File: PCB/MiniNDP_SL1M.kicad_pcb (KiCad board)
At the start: 2 copper layers, 60 x 34 mm, 22 parts, among them J1 Conn_02x20_Odd_Even, U1 AS6C8008_TSOPII, U2 HC238, U3 HC4040, U4 ABT841

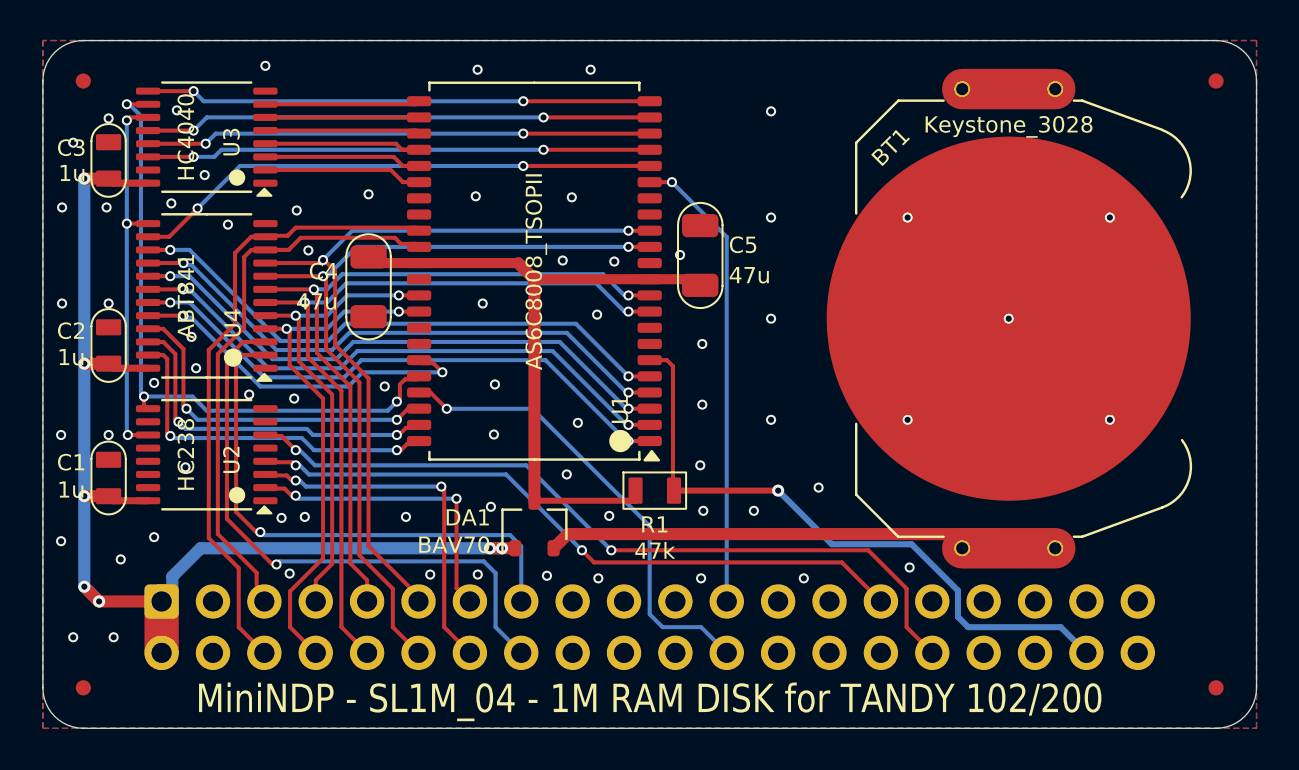
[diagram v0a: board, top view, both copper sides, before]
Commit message: minindp ez1m sl1m ez512 u1m pcbs trace spacing & gnd paths
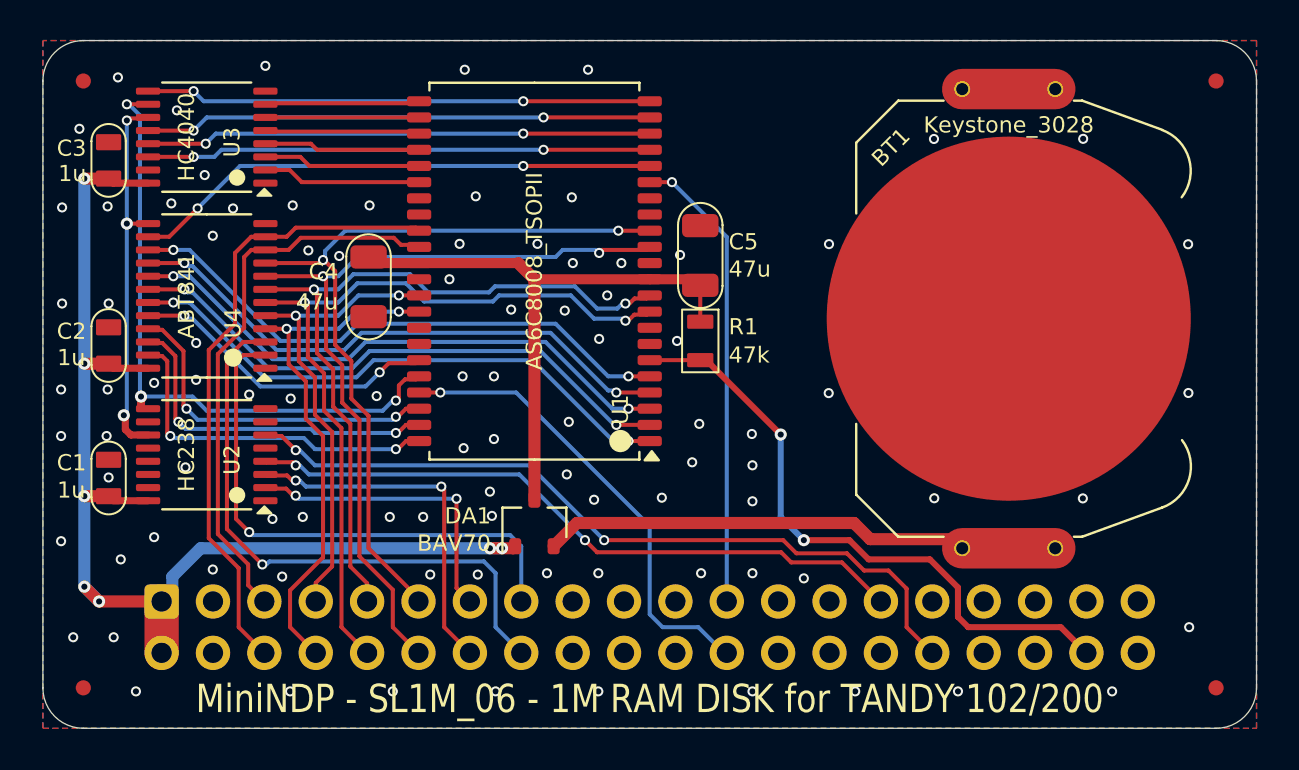
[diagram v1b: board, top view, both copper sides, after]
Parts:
- moved R1 7.73 mm to (154.4, 100.9), turned to -90 degrees
- moved DA1 0.10 mm to (146.2, 109.9)
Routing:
- net VMEM: track 33.5 -> 29.7 mm
- net /A13: track 17.7 -> 15.4 mm
- net +BATT: track 23.1 -> 21.2 mm
- net /RAMRST: track 31.9 -> 30.8 mm, vias 1 -> 2
- net /AD5: track 36.3 -> 37.1 mm
- net /AD4: track 38.6 -> 39.2 mm
- net GND: vias 69 -> 94

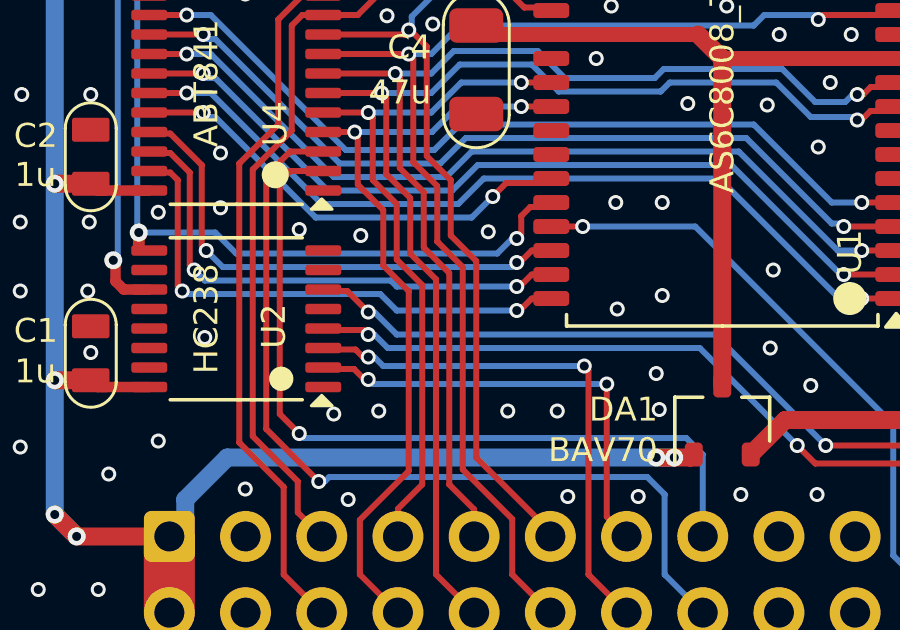
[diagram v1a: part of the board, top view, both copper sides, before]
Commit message: rename breadboard, sl1m trace spacing & silkscreen
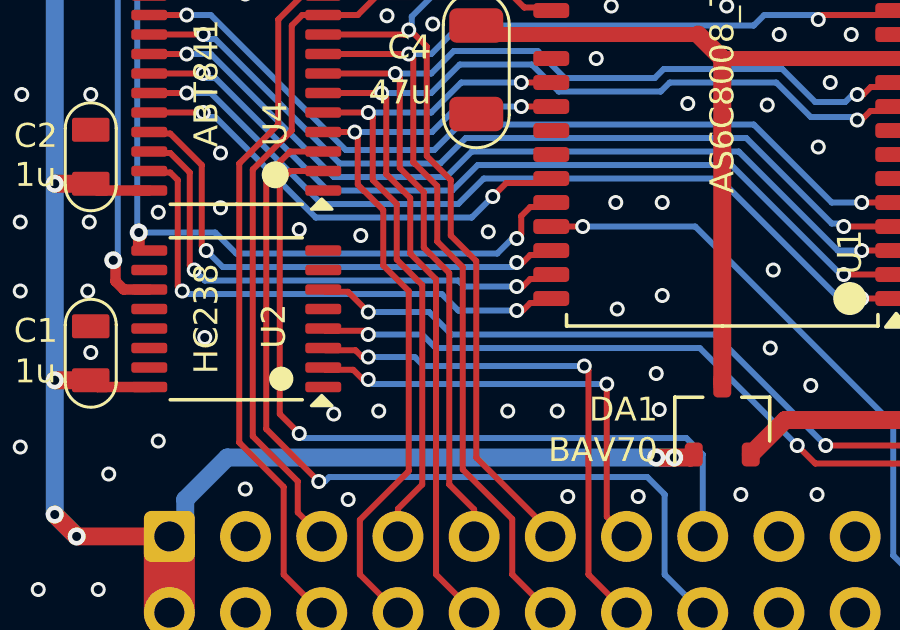
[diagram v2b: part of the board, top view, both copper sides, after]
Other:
- board text added: "To reinstall RAMDSK from device after hard reset. RAMxxx.CO must be the first file in bank 0."
- board text removed: "Bootstrap RAMDSK from BANK 0. For BANK 1 change OUT129 to OUT133. RAM100.CO or RAM200.CO must be the first file in the bank."

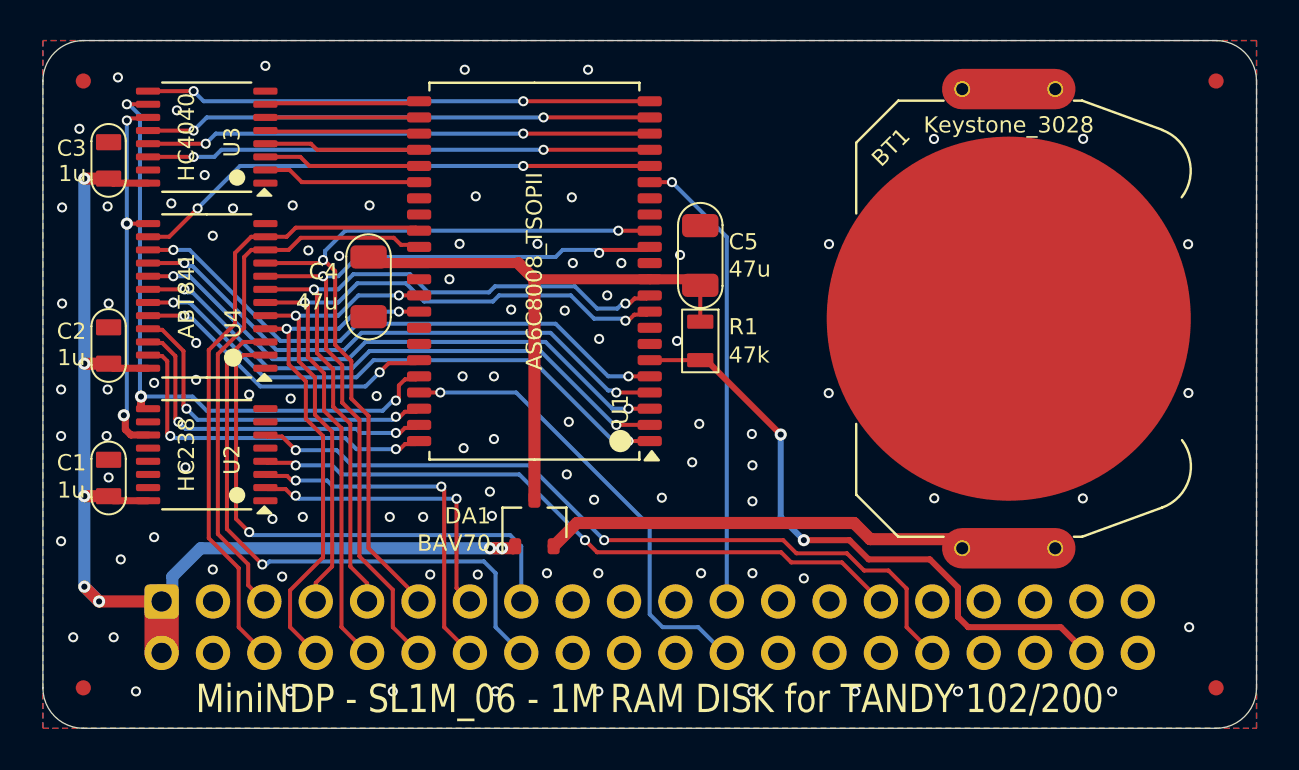
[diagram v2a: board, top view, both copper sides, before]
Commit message: sl1m fillet tracks
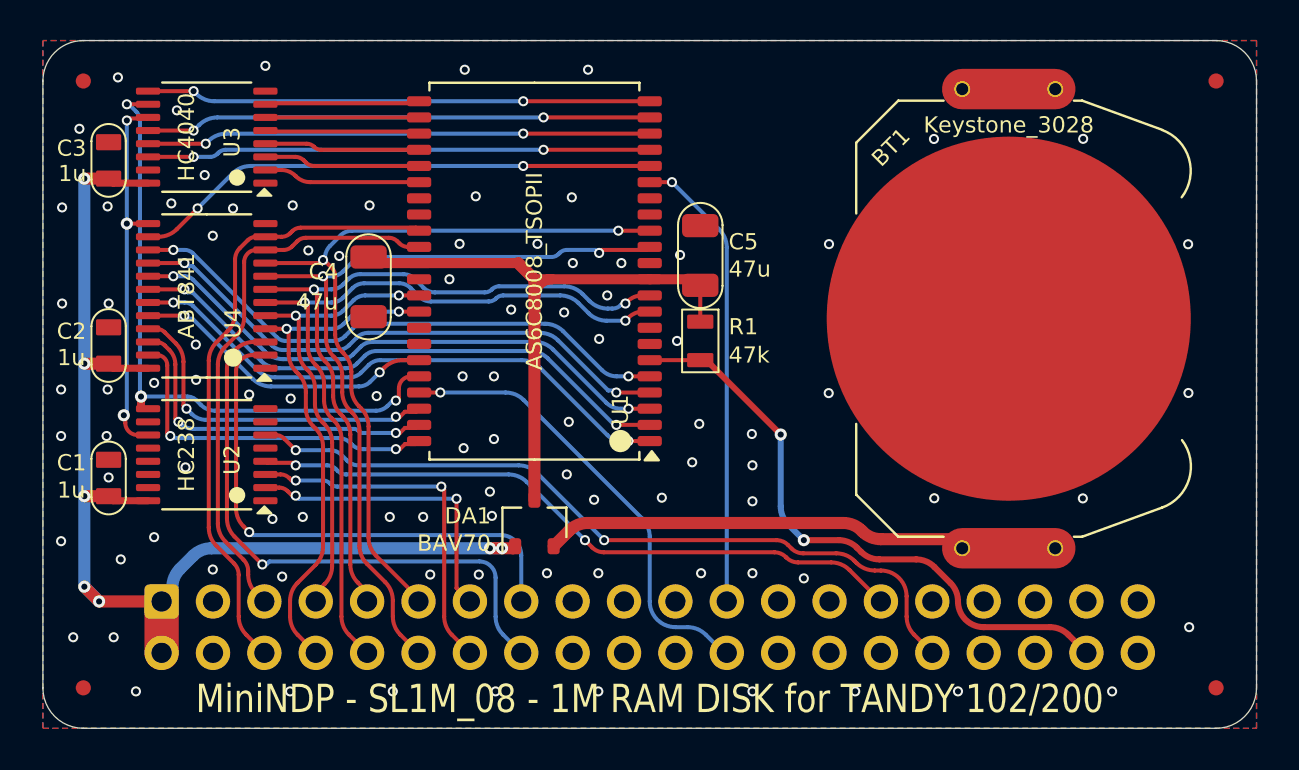
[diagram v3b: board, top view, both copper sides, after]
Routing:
- net /RAMRST: track 30.8 -> 30.1 mm
- net /AD5: track 37.1 -> 36.3 mm
- net /AD4: track 39.2 -> 38.5 mm
- net /AD6: track 40.3 -> 39.7 mm
- net /AD2: track 25.9 -> 25.4 mm

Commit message: sl1m fine tune pcb trace gaps and & fillets
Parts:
- moved R1 0.25 mm to (154.4, 101.1)
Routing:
- net VMEM: track 29.7 -> 28.1 mm
- net GND: vias 94 -> 93

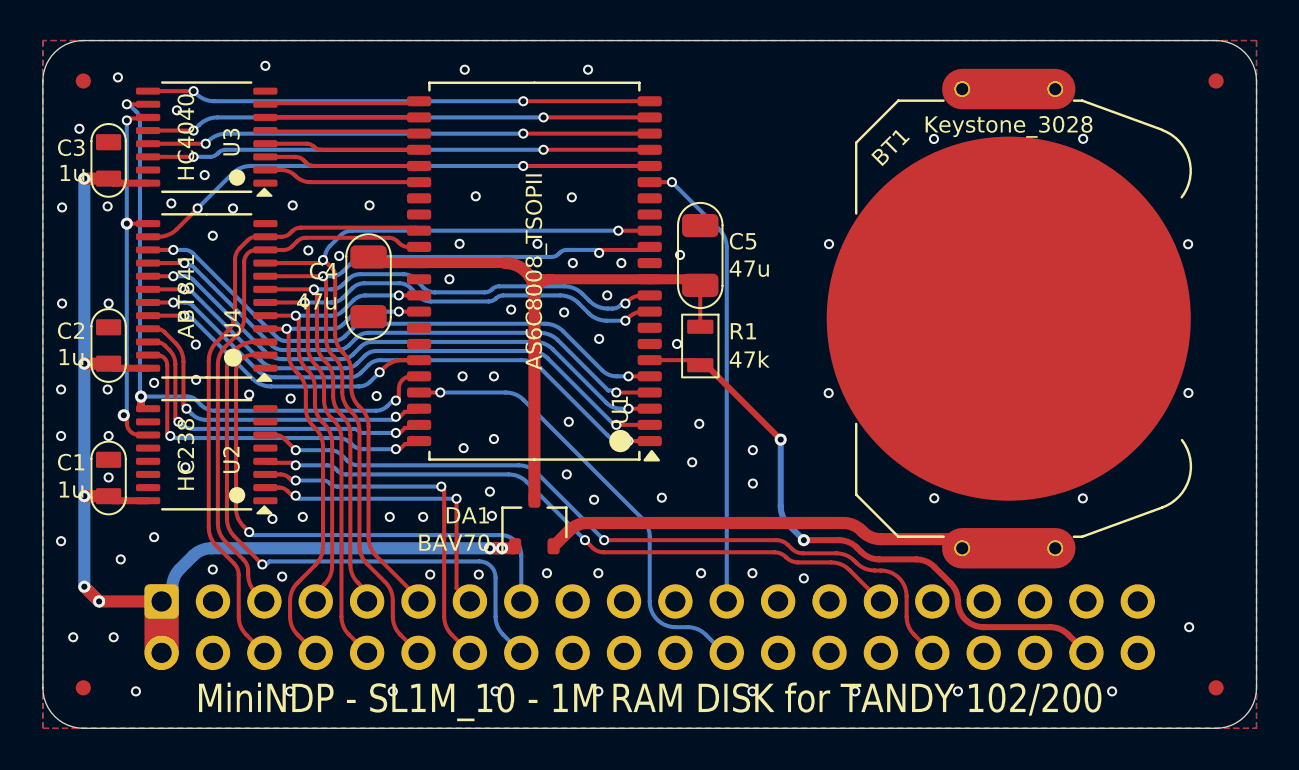
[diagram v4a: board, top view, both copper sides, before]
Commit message: sl1m 014 trace art, silkscreen
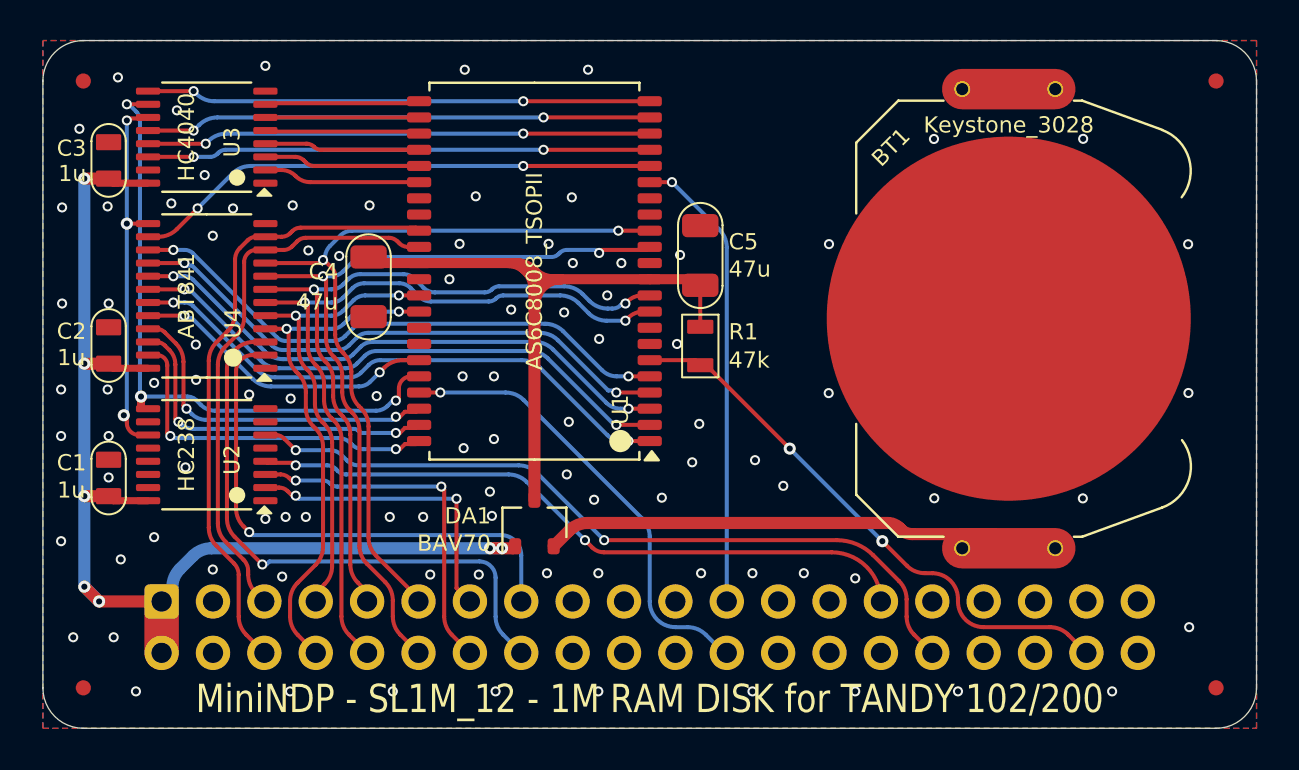
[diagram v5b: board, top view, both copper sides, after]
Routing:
- net +BATT: track 21.0 -> 25.7 mm
- net VMEM: track 28.1 -> 32.4 mm
- net /RAMRST: track 29.9 -> 27.8 mm
- net GND: vias 93 -> 95
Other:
- board text added: "BASIC to bootstrap RAMxxx.CO previously saved as the first file in bank 0"
- board text removed: "To reinstall RAMDSK from device after hard reset. RAMxxx.CO must be the first file in bank 0."

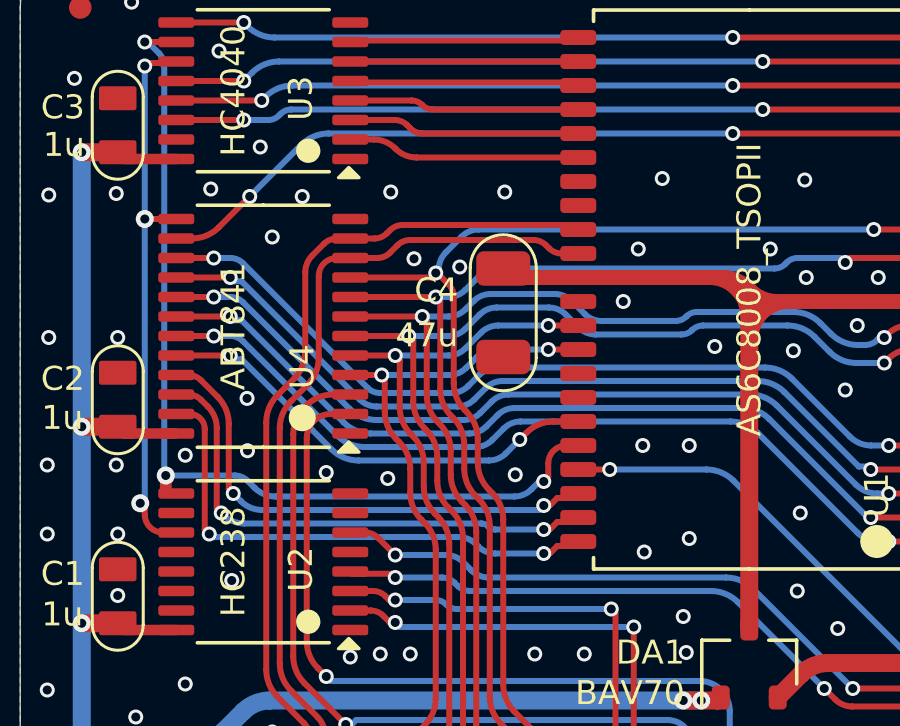
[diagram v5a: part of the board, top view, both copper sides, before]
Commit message: ez256 compatible with 128k sram
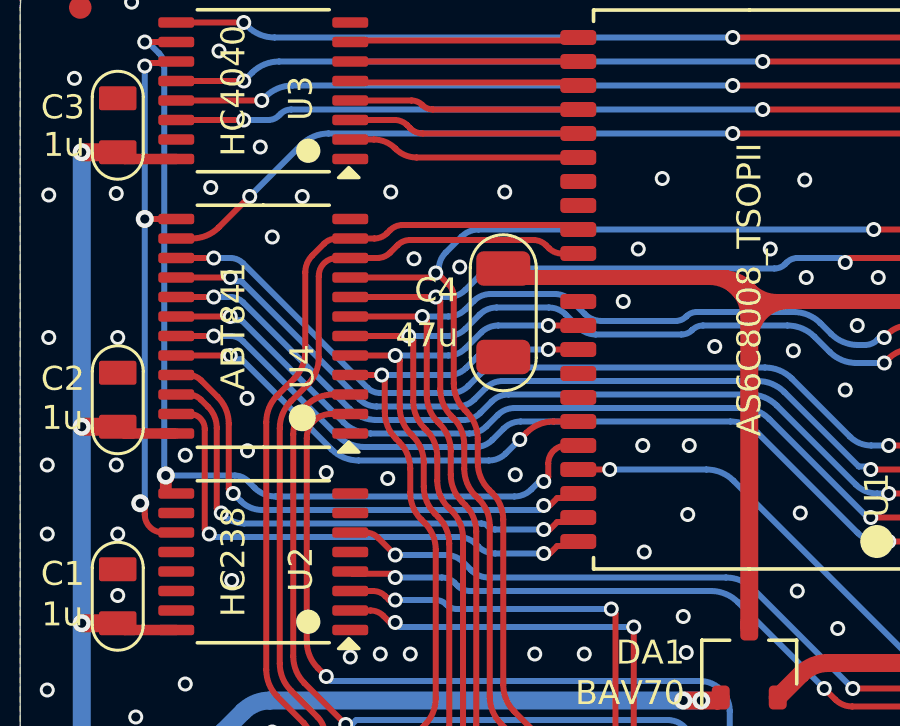
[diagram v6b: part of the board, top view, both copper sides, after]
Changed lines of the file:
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@@
 	)
 	(via
-		(at 128.3 94.075)
+		(at 128.3 94.025)
 		(size 0.5)
 		(drill 0.3)
@@
 	)
 	(via
-		(at 144.25 105.725)
-		(size 0.5)
-		(drill 0.3)
+		(at 144.2 104.925)
+		(size 0.5)
+		(drill 0.3)

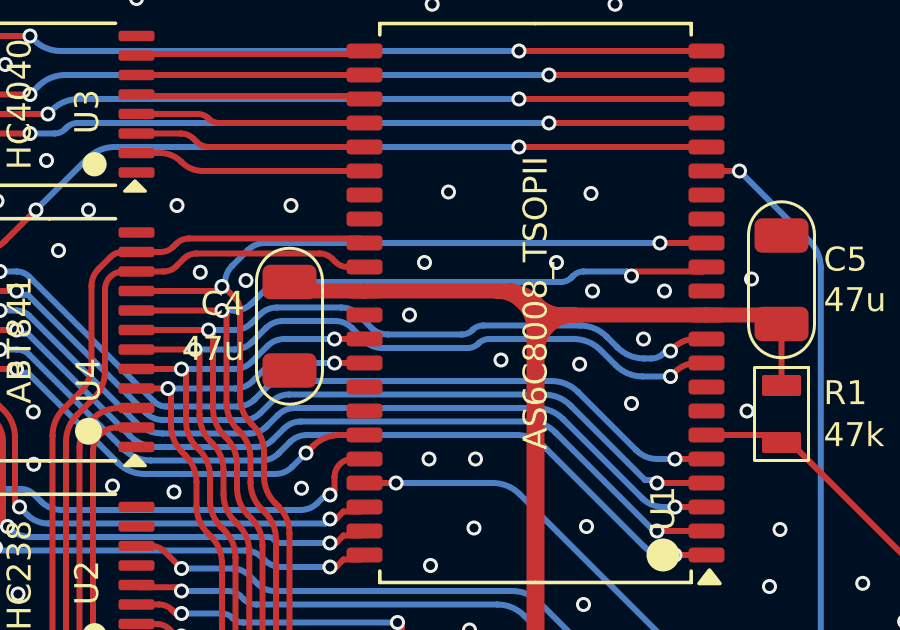
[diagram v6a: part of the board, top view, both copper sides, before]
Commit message: T512 power traces
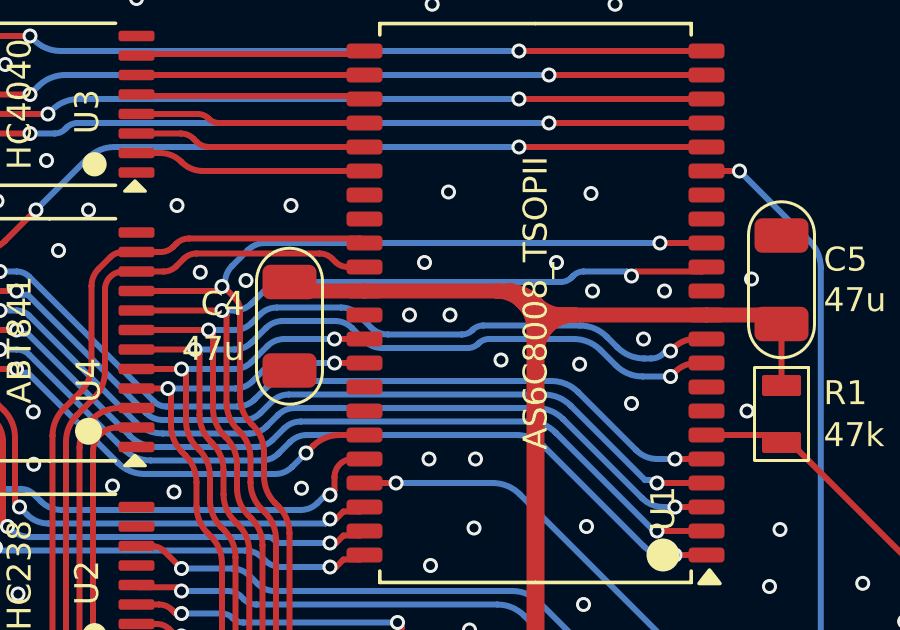
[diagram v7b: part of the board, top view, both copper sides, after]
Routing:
- net GND: vias 95 -> 96
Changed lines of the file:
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@@
+	)
+	(via
+		(at 143.4 97.825)
+		(size 0.5)
+		(drill 0.3)
+		(layers "F.Cu" "B.Cu")
+		(free yes)
+		(net 1)
 	)
 	(via

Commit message: fix tssop-24 model, update cover models
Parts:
- U4: footprint 000_LOCAL:TSSOP-24_4.4x7.8mm_P0.65mm -> 000_LOCAL:TSSOP-24
